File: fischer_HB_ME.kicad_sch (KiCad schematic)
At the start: 6 parts

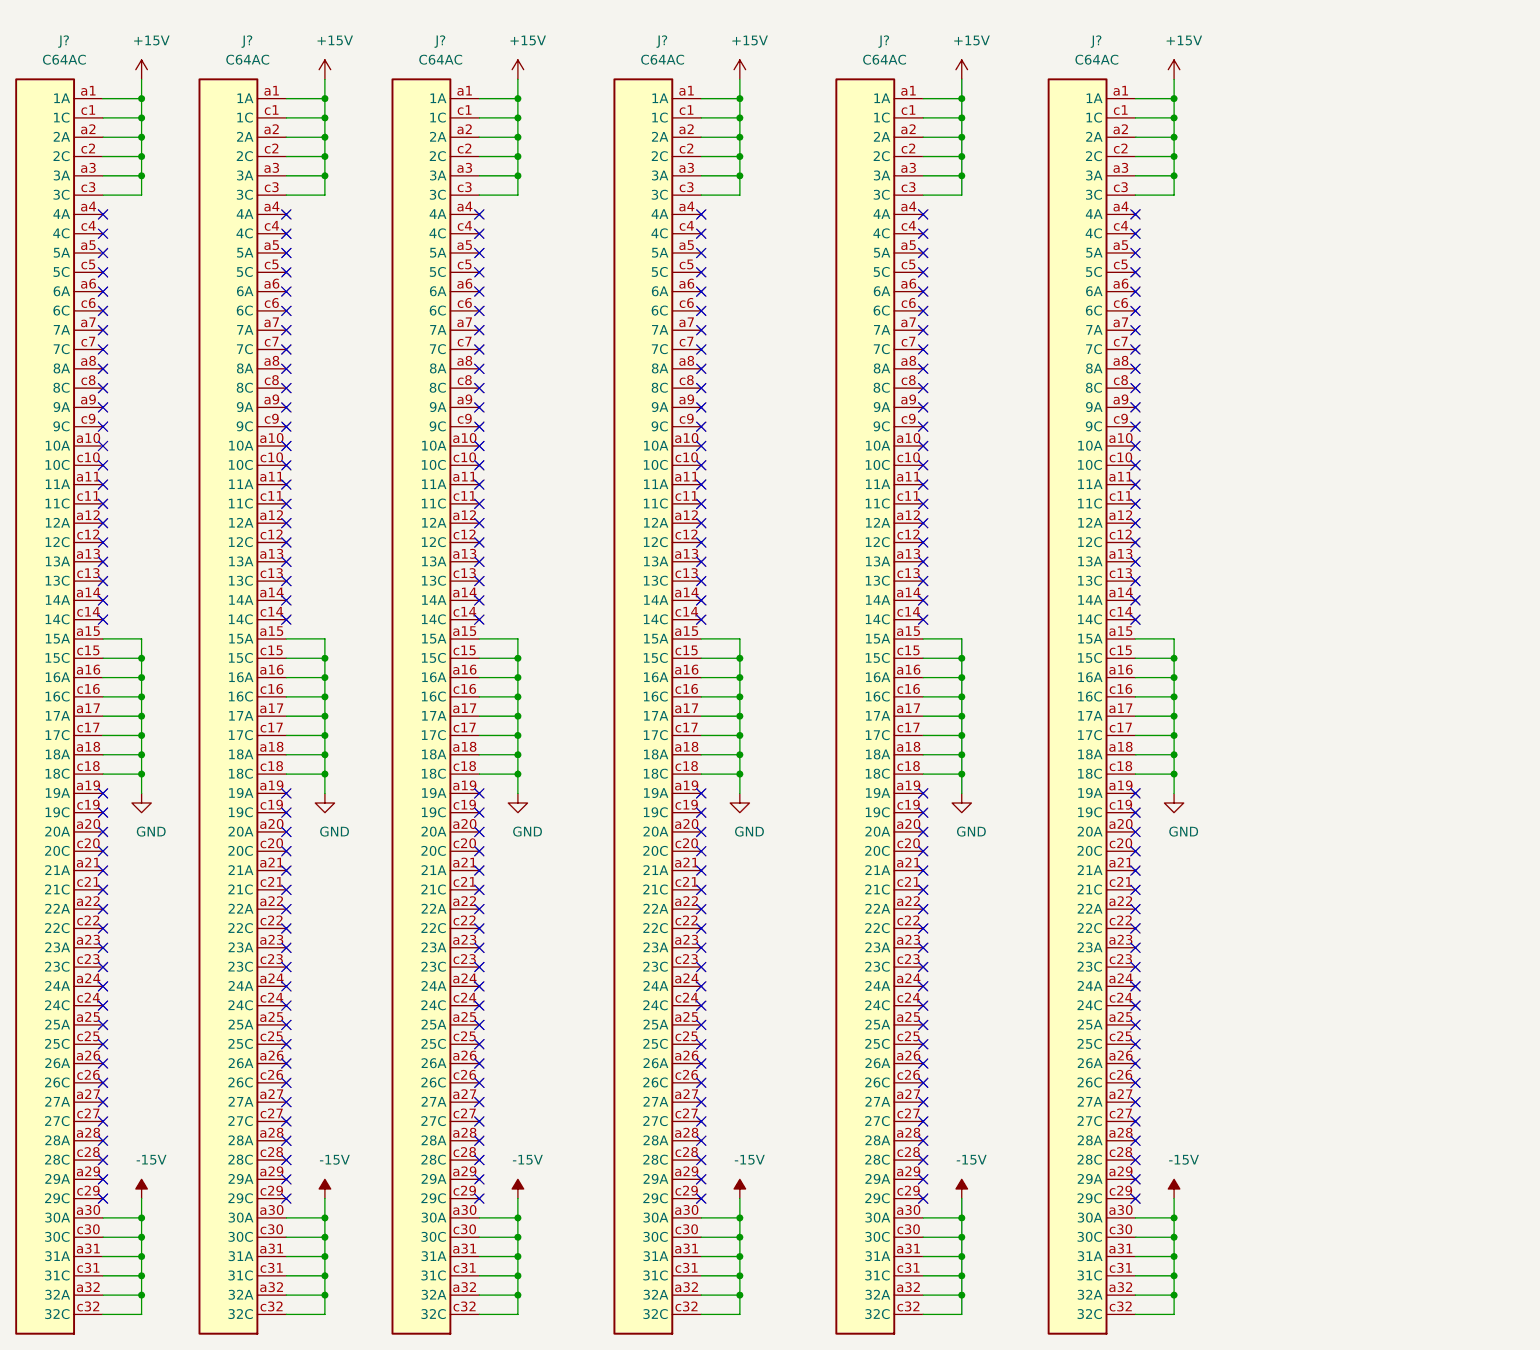
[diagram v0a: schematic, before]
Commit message: Added an input protection circuit Added CI
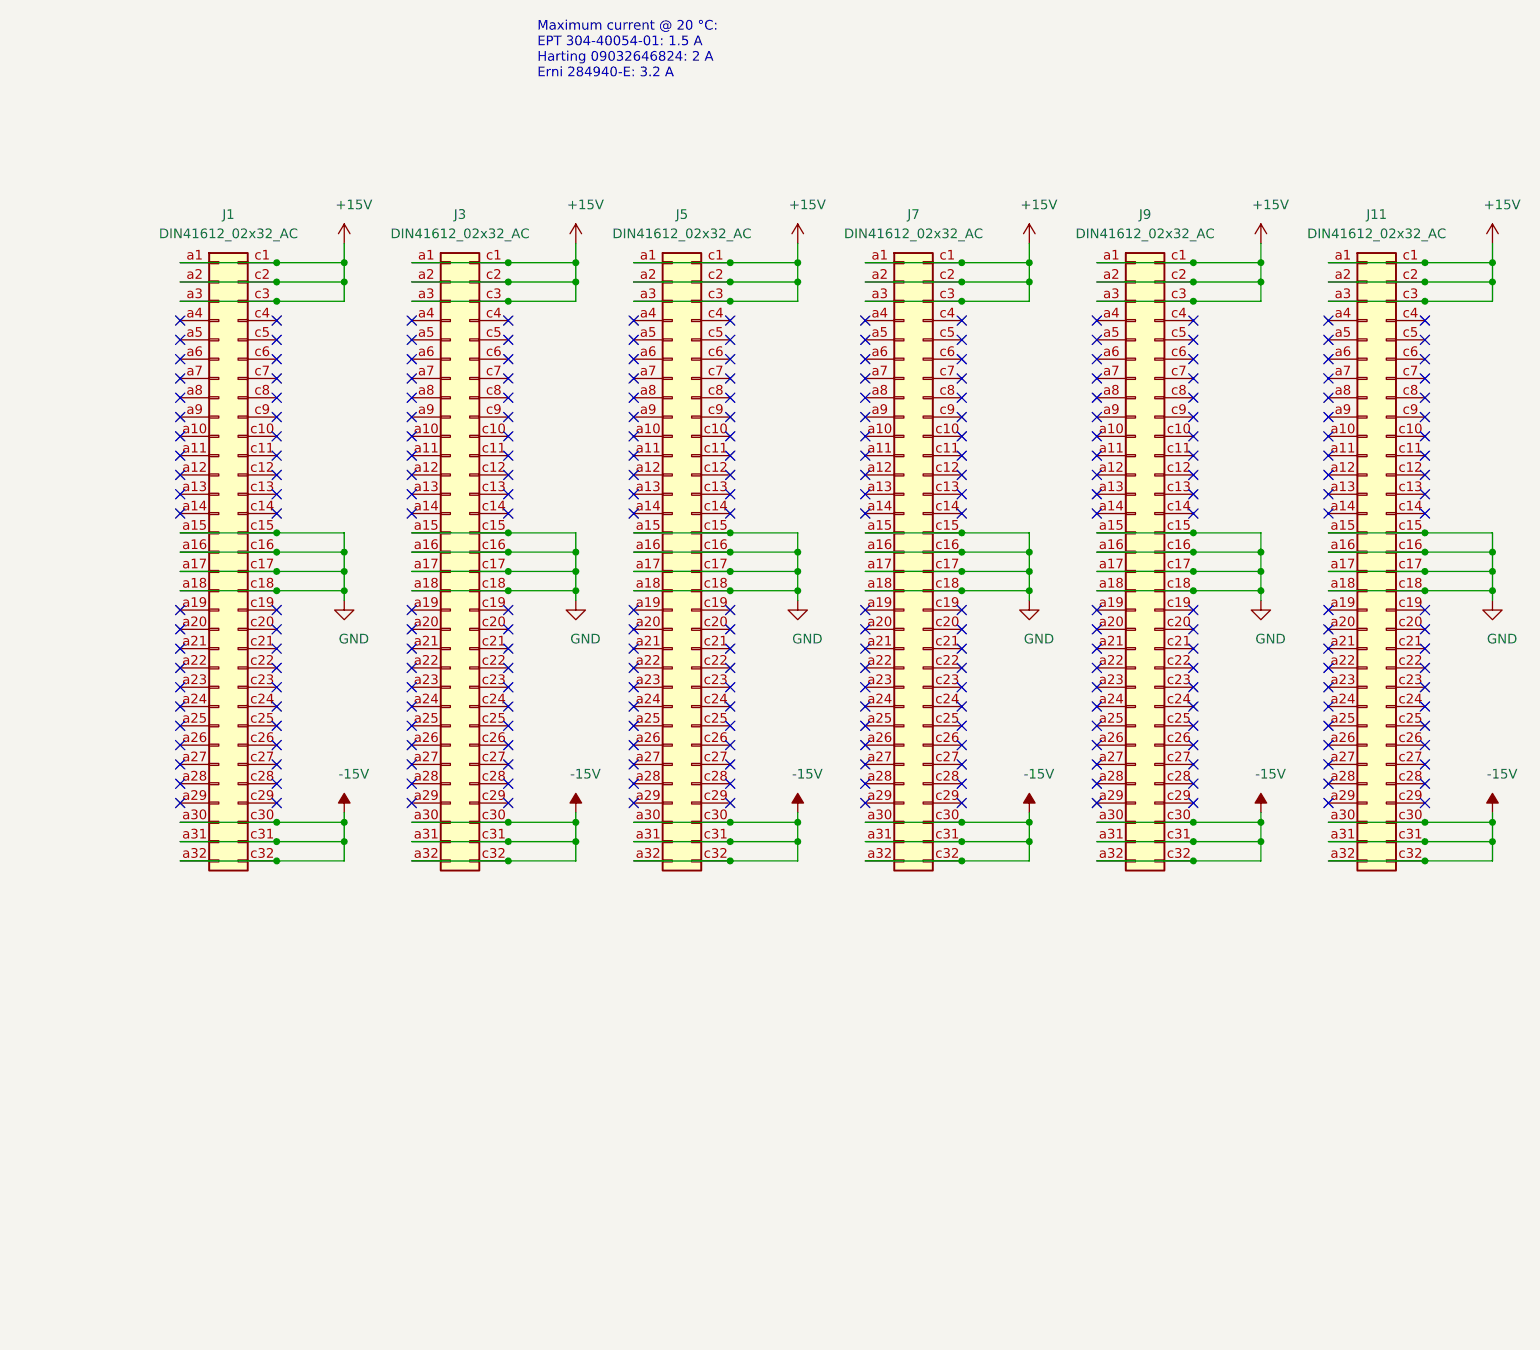
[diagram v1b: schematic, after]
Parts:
- removed J? (x6): C64AC, Connector_DIN:DIN41612_C_2x32_Female_Vertical_THT, symbol Connector_DIN:C64AC
- added J1, J11, J3, J5, J7, J9: DIN41612_02x32_AC, Connector_DIN:DIN41612_C_2x32_Female_Vertical_THT, symbol Connector:DIN41612_02x32_AC
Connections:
- net +15V: now also J1.a1 (Pin_a1), J1.a2 (Pin_a2), J1.a3 (Pin_a3), J1.c1 (Pin_c1), J1.c2 (Pin_c2), J1.c3 (Pin_c3), J11.a1 (Pin_a1), J11.a2 (Pin_a2), J11.a3 (Pin_a3), J11.c1 (Pin_c1), J11.c2 (Pin_c2), J11.c3 (Pin_c3), J3.a1 (Pin_a1), J3.a2 (Pin_a2), J3.a3 (Pin_a3), J3.c1 (Pin_c1), J3.c2 (Pin_c2), J3.c3 (Pin_c3), J5.a1 (Pin_a1), J5.a2 (Pin_a2), J5.a3 (Pin_a3), J5.c1 (Pin_c1), J5.c2 (Pin_c2), J5.c3 (Pin_c3), J7.a1 (Pin_a1), J7.a2 (Pin_a2), J7.a3 (Pin_a3), J7.c1 (Pin_c1), J7.c2 (Pin_c2), J7.c3 (Pin_c3), J9.a1 (Pin_a1), J9.a2 (Pin_a2), J9.a3 (Pin_a3), J9.c1 (Pin_c1), J9.c2 (Pin_c2), J9.c3 (Pin_c3)
- net -15V: now also J1.a30 (Pin_a30), J1.a31 (Pin_a31), J1.a32 (Pin_a32), J1.c30 (Pin_c30), J1.c31 (Pin_c31), J1.c32 (Pin_c32), J11.a30 (Pin_a30), J11.a31 (Pin_a31), J11.a32 (Pin_a32), J11.c30 (Pin_c30), J11.c31 (Pin_c31), J11.c32 (Pin_c32), J3.a30 (Pin_a30), J3.a31 (Pin_a31), J3.a32 (Pin_a32), J3.c30 (Pin_c30), J3.c31 (Pin_c31), J3.c32 (Pin_c32), J5.a30 (Pin_a30), J5.a31 (Pin_a31), J5.a32 (Pin_a32), J5.c30 (Pin_c30), J5.c31 (Pin_c31), J5.c32 (Pin_c32), J7.a30 (Pin_a30), J7.a31 (Pin_a31), J7.a32 (Pin_a32), J7.c30 (Pin_c30), J7.c31 (Pin_c31), J7.c32 (Pin_c32), J9.a30 (Pin_a30), J9.a31 (Pin_a31), J9.a32 (Pin_a32), J9.c30 (Pin_c30), J9.c31 (Pin_c31), J9.c32 (Pin_c32)
- net GND: now also J1.a15 (Pin_a15), J1.a16 (Pin_a16), J1.a17 (Pin_a17), J1.a18 (Pin_a18), J1.c15 (Pin_c15), J1.c16 (Pin_c16), J1.c17 (Pin_c17), J1.c18 (Pin_c18), J11.a15 (Pin_a15), J11.a16 (Pin_a16), J11.a17 (Pin_a17), J11.a18 (Pin_a18), J11.c15 (Pin_c15), J11.c16 (Pin_c16), J11.c17 (Pin_c17), J11.c18 (Pin_c18), J3.a15 (Pin_a15), J3.a16 (Pin_a16), J3.a17 (Pin_a17), J3.a18 (Pin_a18), J3.c15 (Pin_c15), J3.c16 (Pin_c16), J3.c17 (Pin_c17), J3.c18 (Pin_c18), J5.a15 (Pin_a15), J5.a16 (Pin_a16), J5.a17 (Pin_a17), J5.a18 (Pin_a18), J5.c15 (Pin_c15), J5.c16 (Pin_c16), J5.c17 (Pin_c17), J5.c18 (Pin_c18), J7.a15 (Pin_a15), J7.a16 (Pin_a16), J7.a17 (Pin_a17), J7.a18 (Pin_a18), J7.c15 (Pin_c15), J7.c16 (Pin_c16), J7.c17 (Pin_c17), J7.c18 (Pin_c18), J9.a15 (Pin_a15), J9.a16 (Pin_a16), J9.a17 (Pin_a17), J9.a18 (Pin_a18), J9.c15 (Pin_c15), J9.c16 (Pin_c16), J9.c17 (Pin_c17), J9.c18 (Pin_c18)
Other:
- note added: "Maximum current @ 20 °C: EPT 304-40054-01: 1.5 A Harting 09032646824: 2 A Erni 284940-E: 3.2 A"
- title: 19" DIN 41612 Backplane -> Fischer HB ME 14 DIN connector configuration
